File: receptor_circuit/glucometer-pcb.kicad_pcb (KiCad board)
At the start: 2 copper layers, 22 parts, among them IC1 RC4558IP, IC2 LM1458N, IC3 RC4558IP, U1 ESP32_DevKit_V1_DOIT

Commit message: change name
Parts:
- removed BZ1: Buzzer, Buzzer_Beeper:MagneticBuzzer_Kingstate_KCG0601
- removed the D1 at (121.1, 136.9)
- removed D2: LED, LED_THT:LED_D3.0mm_FlatTop
- removed the R3 at (114.7, 115.1)
- removed the R4 at (114.6, 119.1)
- removed U1: ESP32_DevKit_V1_DOIT, esp32_devkit_v1_doit:esp32_devkit_v1_doit_own_ESP
- added REF**: MountingHole_2.2mm_M2_ISO7380, MountingHole:MountingHole_2.2mm_M2_ISO7380, F.Cu at (206.9, 121.8)
- added REF**: MountingHole_2.2mm_M2_ISO7380, MountingHole:MountingHole_2.2mm_M2_ISO7380, F.Cu at (177.1, 175.4)
- added TP3: SIGNAL_OUT, TestPoint:TestPoint_Keystone_5015_Micro-Minature, F.Cu at (198.6, 121.8)
- moved TP2 76.4 mm to (189.8, 121.8), turned to 180 degrees
- moved TP1 65.2 mm to (180.5, 121.8), turned to 180 degrees
- moved D1 56.7 mm to (191.6, 174.8)
- moved C1 53.5 mm to (191.6, 136.5)
- moved R4 52.6 mm to (178.5, 164.2)
- moved C2 52.2 mm to (182.8, 159.8)
- moved C3 52.2 mm to (190.4, 131.4)
- moved R1 52.0 mm to (204.7, 127.1)
- moved R2 52.0 mm to (204.8, 130.9)
- moved R3 52.0 mm to (193.9, 149.0)
- moved R5 52.0 mm to (198.7, 159.9)
- moved R6 52.0 mm to (198.6, 156.7)
- moved R7 52.0 mm to (201.0, 152.4)
- moved IC1 52.0 mm to (201.8, 139.4)
- moved IC2 52.0 mm to (179.2, 154.9)
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- renumbered D3 to D1, R5 to R3, R6 to R4, R7 to R5, R8 to R6, R9 to R7
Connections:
- net SIGNAL_OUT renamed Net-(IC3-Pad6)
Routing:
- net Net-(BZ1-Pad1): track 79.1 -> 0.00 mm
- net Net-(R3-Pad2): track 77.4 -> 0.00 mm
- net VCC: track 176.5 -> 111.8 mm
- net Net-(D2-Pad1): track 54.9 -> 0.00 mm
- net Net-(D2-Pad2): track 37.6 -> 0.00 mm
- net Net-(D1-Pad2): track 19.1 -> 0.00 mm
- net Net-(IC3-Pad6): track 98.8 -> 84.2 mm
- net GND: track 112.7 -> 101.5 mm
- net Net-(BZ1-Pad2): track 9.27 -> 0.00 mm
- net /PWD_1.65: track 102.6 -> 96.3 mm
- net Net-(C2-Pad2): track 50.4 -> 55.9 mm
- net Net-(C1-Pad1): track 23.0 -> 19.4 mm
- net /SIGNAL_1: track 71.2 -> 69.6 mm
- net /SIGNAL_2: track 17.5 -> 16.4 mm
- net Net-(C2-Pad1): track 22.1 -> 23.0 mm
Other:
- board outline added: 36.5 x 59.9 mm

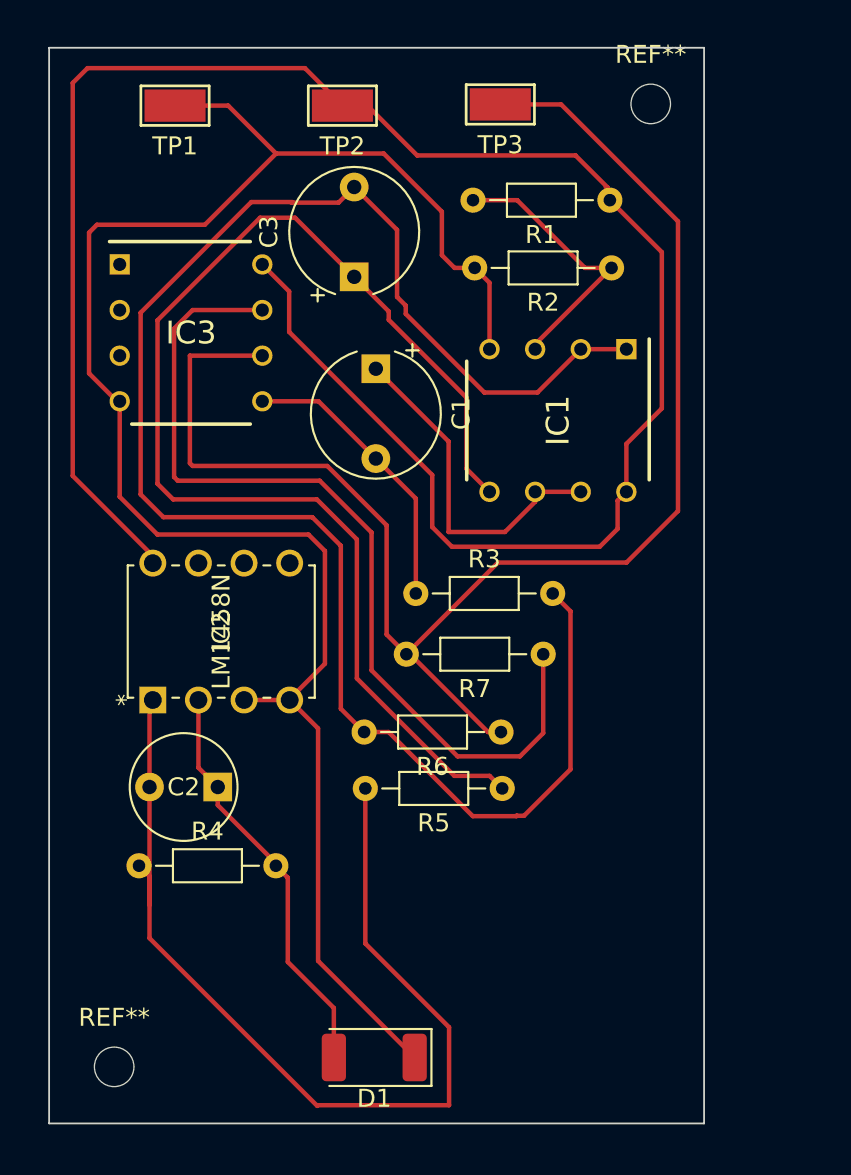
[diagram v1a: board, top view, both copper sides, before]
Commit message: replace top wires with bottom wires
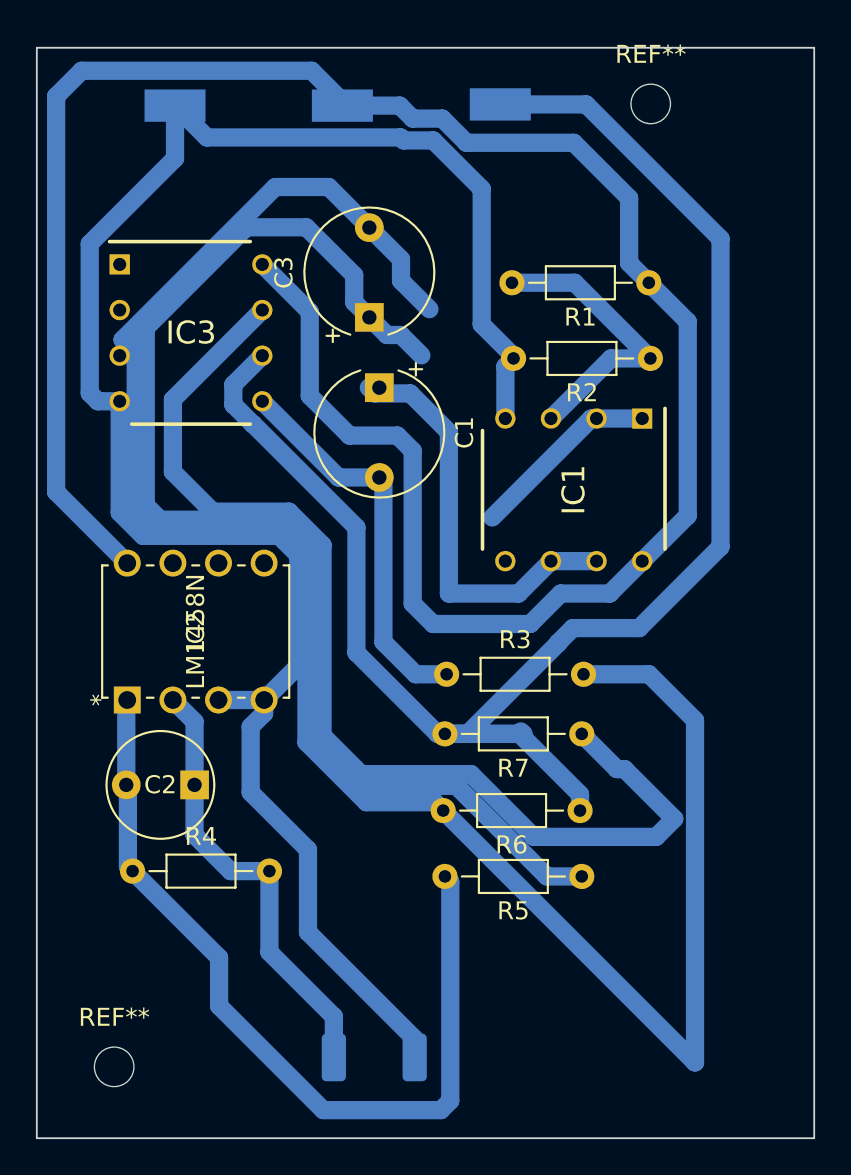
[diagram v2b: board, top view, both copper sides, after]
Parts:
- D1, TP1, TP2, TP3: moved to B.Cu
- moved R5 6.61 mm to (203.1, 164.8)
- moved R6 6.20 mm to (203.0, 161.1)
- moved R2 5.48 mm to (206.9, 135.9)
- moved R1 5.08 mm to (206.8, 131.7)
- moved R7 4.93 mm to (203.1, 156.8)
- moved R3 4.82 mm to (195.6, 153.5)
- moved IC1 3.96 mm to (202.7, 143.2)
- moved C3 2.41 mm to (191.3, 133.6)
- moved IC2 1.42 mm to (177.8, 154.9)
- moved C2 1.30 mm to (181.5, 159.7)
- moved C1 1.07 mm to (191.8, 137.6)
- moved R4 0.47 mm to (178.1, 164.5)
- turned TP1 to 0 degrees
- turned TP2 to 0 degrees
- turned TP3 to 0 degrees
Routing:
- net /PWD_1.65: track 96.3 -> 121.7 mm
- net VCC: track 111.8 -> 124.4 mm
- net Net-(IC3-Pad7): track 50.0 -> 61.2 mm
- net Net-(IC3-Pad6): track 84.2 -> 93.4 mm
- net Net-(C2-Pad2): track 55.9 -> 47.3 mm
- net /SIGNAL_2: track 16.4 -> 21.9 mm
- net Net-(C1-Pad1): track 19.4 -> 23.4 mm
- net GND: track 101.5 -> 105.0 mm
- net Net-(C2-Pad1): track 23.0 -> 24.9 mm
- net Net-(IC1-Pad3): track 15.6 -> 16.4 mm
- net /SIGNAL_1: track 69.6 -> 70.4 mm
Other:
- board size 36.5 x 59.9 mm -> 43.3 x 60.7 mm

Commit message: last update reciver circuit pcb
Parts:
- moved R2 21.0 mm to (205.6, 115.0)
- moved REF** 18.5 mm to (209.9, 103.5)
- moved IC1 16.3 mm to (201.3, 127.0)
- moved R1 15.5 mm to (198.0, 119.0), turned to 0 degrees
- moved TP3 14.1 mm to (205.0, 109.2)
- moved C3 14.1 mm to (184.3, 121.4), turned to 180 degrees
- moved TP2 13.1 mm to (193.3, 109.2)
- moved TP1 12.7 mm to (182.1, 109.2)
- moved R3 5.51 mm to (198.6, 148.9)
- moved C1 4.95 mm to (191.9, 132.6)
- moved R7 4.88 mm to (206.0, 152.9)
- moved R6 3.59 mm to (206.3, 159.7)
- moved R5 3.22 mm to (206.3, 164.7)
- moved REF** 2.48 mm to (174.6, 175.5)
- moved IC3 0.96 mm to (181.3, 133.5)
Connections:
- C1 pad 1: Net-(C1-Pad1) -> /SIGNAL_1
- IC1 pad 6: Net-(C1-Pad1) -> /SIGNAL_1
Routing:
- net Net-(C1-Pad1): track 23.4 -> 0.00 mm
- net /SIGNAL_1: track 70.4 -> 85.2 mm
- net VCC: track 124.4 -> 135.6 mm
- net GND: track 105.0 -> 113.5 mm
- net Net-(IC3-Pad6): track 93.4 -> 86.4 mm
- net Net-(IC1-Pad3): track 16.4 -> 12.2 mm
- net /PWD_1.65: track 121.7 -> 118.1 mm
- net Net-(IC3-Pad7): track 61.2 -> 58.6 mm
- net Net-(C2-Pad2): track 47.3 -> 48.8 mm
- net /SIGNAL_2: track 21.9 -> 21.1 mm
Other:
- board size 43.3 x 60.7 mm -> 43.1 x 79.4 mm

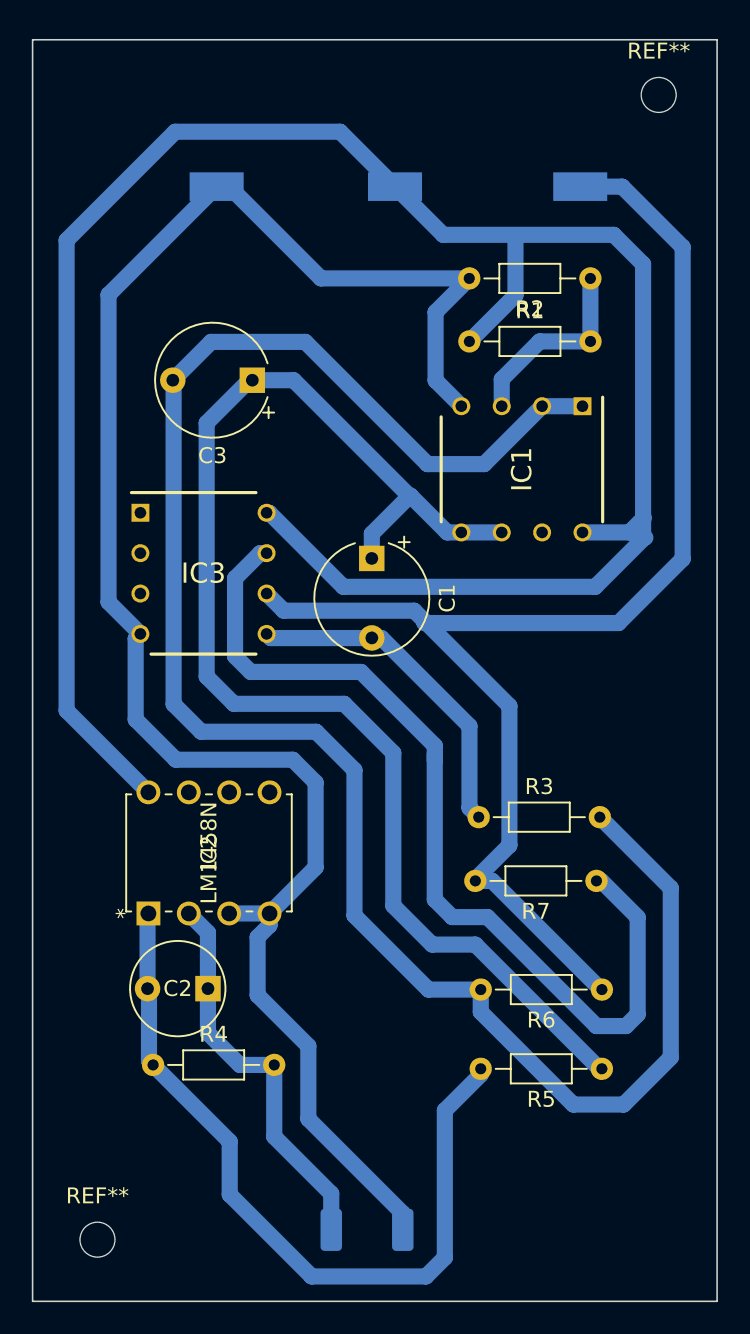
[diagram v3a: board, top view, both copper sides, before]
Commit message: filled pcb
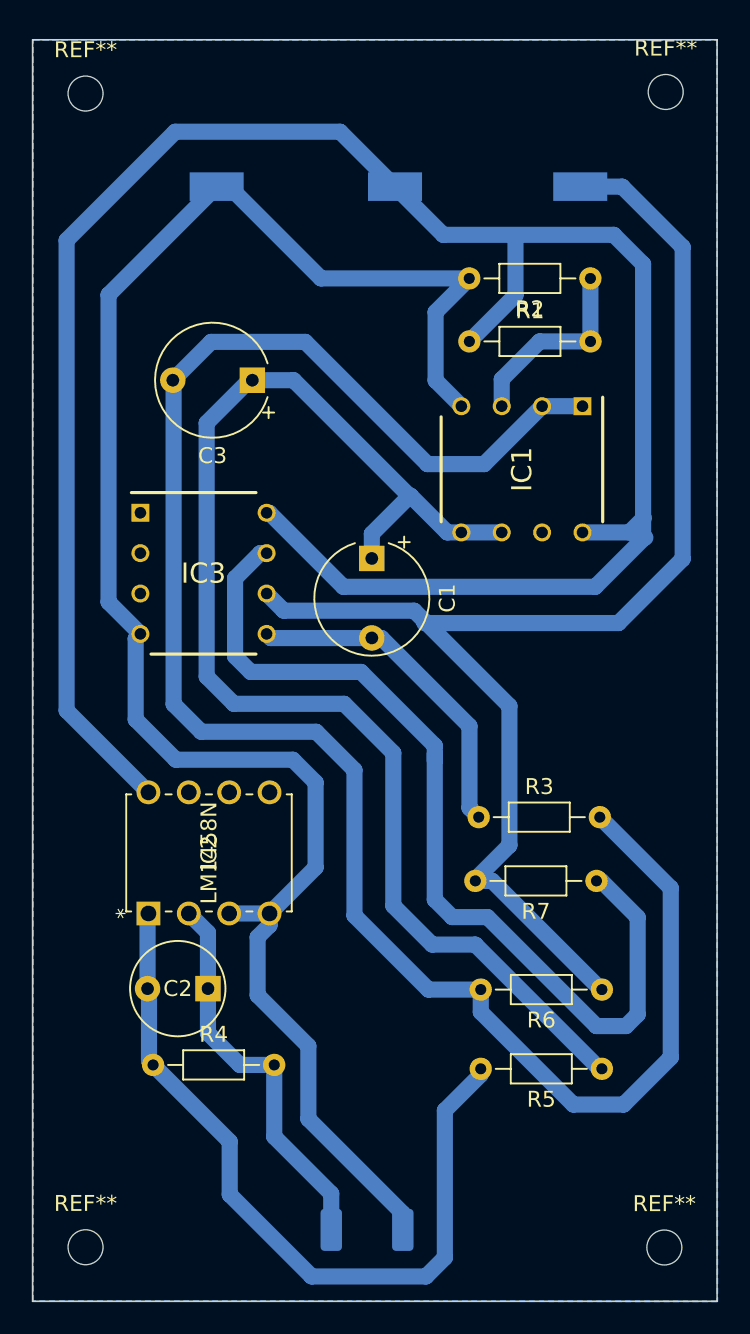
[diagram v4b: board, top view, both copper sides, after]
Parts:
- added REF**: MountingHole_2.2mm_M2_ISO7380, MountingHole:MountingHole_2.2mm_M2_ISO7380, F.Cu at (173.8, 103.4)
- added REF**: MountingHole_2.2mm_M2_ISO7380, MountingHole:MountingHole_2.2mm_M2_ISO7380, F.Cu at (210.3, 176.0)
- moved REF** 0.89 mm to (173.8, 175.9)
- moved REF** 0.48 mm to (210.3, 103.3)
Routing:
- added copper zone on B.Cu, net GND
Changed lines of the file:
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@@
       (net 7 "VCC") (pinfunction "V+") (pintype "passive"))
+  )
+  (footprint "MountingHole:MountingHole_2.2mm_M2_ISO7380" (layer "F.Cu")
+    (at 173.845921 103.364595)
+    (descr "Mounting Hole 2.2mm, no annular, M2, ISO7380")
+    (tags "mounting hole 2.2mm no annular m2 iso7380")
+    (attr exclude_from_pos_files exclude_from_bom)
+    (fp_text reference "REF**" (at 0 -2.75) (layer "F.SilkS")
+      (effects (font (size 1 1) (thickness 0.15)))
+    )
+    (fp_text value "MountingHole_2.2mm_M2_ISO7380" (at 0 2.75) (layer "F.Fab")
+      (effects (font (size 1 1) (thickness 0.15)))
+    )
+    (fp_text user "${REFERENCE}" (at 0 0) (layer "F.Fab")
+      (effects (font (size 1 1) (thickness 0.15)))
+    )
+    (fp_circle (center 0 0) (end 1.75 0) (layer "Cmts.User") (width 0.15) (fill none))
+    (fp_circle (center 0 0) (end 2 0) (layer "F.CrtYd") (width 0.05) (fill none))
+    (pad "" np_thru_hole circle (at 0 0) (size 2.2 2.2) (drill 2.2) (layers *.Cu *.Mask))
+  )
+  (footprint "MountingHole:MountingHole_2.2mm_M2_ISO7380" (layer "F.Cu")
+    (at 210.252776 175.950494)
+    (descr "Mounting Hole 2.2mm, no annular, M2, ISO7380")
+    (tags "mounting hole 2.2mm no annular m2 iso7380")
+    (attr exclude_from_pos_files exclude_from_bom)
+    (fp_text reference "REF**" (at 0 -2.75) (layer "F.SilkS")
+      (effects (font (size 1 1) (thickness 0.15)))
+    )
+    (fp_text value "MountingHole_2.2mm_M2_ISO7380" (at 0 2.75) (layer "F.Fab")
+      (effects (font (size 1 1) (thickness 0.15)))
+    )
+    (fp_text user "${REFERENCE}" (at 0 0) (layer "F.Fab")
+      (effects (font (size 1 1) (thickness 0.15)))
+    )
+    (fp_circle (center 0 0) (end 1.75 0) (layer "Cmts.User") (width 0.15) (fill none))
+    (fp_circle (center 0 0) (end 2 0) (layer "F.CrtYd") (width 0.05) (fill none))
+    (pad "" np_thru_hole circle (at 0 0) (size 2.2 2.2) (drill 2.2) (layers *.Cu *.Mask))
   )
   (footprint "Resistor_THT:R_Axial_DIN0204_L3.6mm_D1.6mm_P7.62mm_Horizontal" (layer "F.Cu")
@@
   )
   (footprint "MountingHole:MountingHole_2.2mm_M2_ISO7380" (layer "F.Cu")
-    (at 209.897992 103.451872)
+    (at 210.33914 103.265307)
     (descr "Mounting Hole 2.2mm, no annular, M2, ISO7380")
     (tags "mounting hole 2.2mm no annular m2 iso7380")
@@
   )
   (footprint "MountingHole:MountingHole_2.2mm_M2_ISO7380" (layer "F.Cu")
-    (at 174.596308 175.458104)
+    (at 173.846036 175.934116)
     (descr "Mounting Hole 2.2mm, no annular, M2, ISO7380")
     (tags "mounting hole 2.2mm no annular m2 iso7380")
@@
   (segment (start 204.961987 109.22) (end 207.602348 109.22) (width 1.016) (layer "B.Cu") (net 17))
   (segment (start 194.516999 135.894274) (end 200.507955 141.88523) (width 1.016) (layer "B.Cu") (net 17))
+  (zone (net 8) (net_name "GND") (layer "B.Cu") (hatch edge 0.508)
+    (connect_pads (clearance 0.508))
+    (min_thickness 0.254) (filled_areas_thickness no)
+    (fill yes (thermal_gap 0.508) (thermal_bridge_width 0.508))
+    (polygon
+      (pts
+        (xy 213.570984 179.31525)
+        (xy 170.534443 179.326242)
+        (xy 170.533435 100.006232)
+        (xy 213.572779 99.993445)
+      )
+    )
+  )
+  (zone (net 8) (net_name "GND") (layer "B.Cu") (hatch edge 0.508)
+    (connect_pads (clearance 1))
+    (min_thickness 0.254) (filled_areas_thickness no)
+    (fill yes (thermal_gap 0.508) (thermal_bridge_width 0.508))
+    (polygon
+      (pts
+        (xy 213.602951 179.355406)
+        (xy 170.538033 179.308857)
+        (xy 170.555419 100.016216)
+        (xy 213.56459 99.97606)
+      )
+    )
+  )
 )

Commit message: fixed PCB
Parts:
- moved REF** 34.6 mm to (175.8, 173.0)
- moved REF** 32.6 mm to (206.3, 172.9)
- moved R4 29.8 mm to (177.3, 124.3), turned to 0 degrees
- moved R3 20.7 mm to (177.3, 120.4)
- moved C2 9.78 mm to (191.4, 128.2), turned to 90 degrees
- moved REF** 8.79 mm to (206.3, 111.1)
- moved REF** 7.94 mm to (175.8, 111.1)
- moved S_OUT1 6.56 mm to (202.5, 115.3)
- moved VCC1 6.12 mm to (192.5, 115.3)
- moved GND1 6.10 mm to (181.4, 115.3)
- moved R2 3.00 mm to (204.3, 162.5)
- moved R5 3.00 mm to (196.6, 146.7)
- moved R6 3.00 mm to (204.3, 157.5)
- moved R7 3.00 mm to (204.0, 150.7)
- moved RECEPTOR_DIODE1 2.55 mm to (191.5, 172.3)
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- renumbered C2 to C1, C3 to C2, C1 to C3, TP1 to GND1, IC2 to LM1458N1, R4 to R1, R5 to R2, R1 to R3, R2 to R4, R3 to R5, IC1 to RC4558IP1, IC3 to RC4558IP2, D1 to RECEPTOR_DIODE1, TP3 to S_OUT1, TP2 to VCC1
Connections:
- C3 pad 1: /SIGNAL_1 -> Net-(C3-Pad1)
- RC4558IP1 pad 6: /SIGNAL_1 -> Net-(C3-Pad1)
- RC4558IP1 pad 7: Net-(C1-Pad1) (its old number) -> Net-(C3-Pad1)
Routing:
- net /SIGNAL_1: track 85.2 -> 66.4 mm
- net /PWD_1.65: track 118.1 -> 102.4 mm
- net VCC: track 135.6 -> 119.9 mm
- net Net-(R3-Pad2): track 12.2 -> 26.1 mm
- net Net-(R6-Pad1): track 86.4 -> 72.7 mm
- net Net-(C3-Pad1): track 0.00 -> 12.3 mm
- net GND: track 113.5 -> 103.5 mm
- net Net-(R7-Pad1): track 58.6 -> 55.5 mm
- net /SIGNAL_2: track 21.1 -> 18.1 mm
- net Net-(C1-Pad2): track 48.8 -> 46.9 mm
- net Net-(C1-Pad1): track 24.9 -> 24.3 mm
- removed copper zone on B.Cu, net GND
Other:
- board size 43.1 x 79.4 mm -> 36.9 x 68.2 mm

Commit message: filled zone
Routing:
- added copper zone on B.Cu, net GND
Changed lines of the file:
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@@
   (segment (start 200.031141 132.634489) (end 198.507094 134.158536) (width 0.25) (layer "B.Cu") (net 4))
   (segment (start 187.93263 140.464412) (end 182.583884 140.464412) (width 0.3) (layer "B.Cu") (net 5))
-  (segment (start 204.297807 162.49408) (end 197.284171 155.480444) (width 0.3) (layer "B.Cu") (net 5))
   (segment (start 204.297807 162.49408) (end 204.153157 162.49408) (width 0.3) (layer "B.Cu") (net 5))
   (segment (start 191.201485 143.733267) (end 187.93263 140.464412) (width 0.3) (layer "B.Cu") (net 5))
@@
   (segment (start 193.882535 155.478452) (end 191.201485 152.797402) (width 0.3) (layer "B.Cu") (net 5))
   (segment (start 197.306235 155.478452) (end 193.882535 155.478452) (width 0.3) (layer "B.Cu") (net 5))
+  (segment (start 204.297807 162.49408) (end 197.284171 155.480444) (width 0.3) (layer "B.Cu") (net 5))
   (segment (start 197.491141 132.634489) (end 193.046426 128.189774) (width 0.25) (layer "B.Cu") (net 5))
   (segment (start 205.187383 164.594522) (end 202.830187 164.594522) (width 0.3) (layer "B.Cu") (net 6))
@@
   (segment (start 205.641516 159.565867) (end 203.944052 159.565867) (width 0.3) (layer "B.Cu") (net 14))
   (segment (start 206.245698 158.961685) (end 205.641516 159.565867) (width 0.3) (layer "B.Cu") (net 14))
+  (zone (net 8) (net_name "GND") (layer "B.Cu") (hatch edge 0.508)
+    (connect_pads (clearance 0.508))
+    (min_thickness 0.254) (filled_areas_thickness no)
+    (fill yes (thermal_gap 0.508) (thermal_bridge_width 0.508))
+    (polygon
+      (pts
+        (xy 209.532853 107.900727)
+        (xy 209.53372 176.101312)
+        (xy 172.642584 176.140236)
+        (xy 172.631586 107.900294)
+      )
+    )
+  )
 )

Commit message: last update
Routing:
- net GND: track 103.5 -> 3.16 mm
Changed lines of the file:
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@@
   (segment (start 206.531781 122.58851) (end 207.250455 123.307184) (width 0.3) (layer "B.Cu") (net 7))
   (segment (start 200.570295 122.58851) (end 206.531781 122.58851) (width 0.3) (layer "B.Cu") (net 7))
-  (segment (start 180.34 127) (end 175.26 127) (width 0.3) (layer "B.Cu") (net 8))
   (segment (start 176.997647 137.651809) (end 177.294626 137.35483) (width 0.3) (layer "B.Cu") (net 8))
-  (segment (start 190.072645 168.581542) (end 193.779544 172.288441) (width 0.3) (layer "B.Cu") (net 8))
-  (segment (start 194.198781 121.402129) (end 197.491141 124.694489) (width 0.3) (layer "B.Cu") (net 8))
-  (segment (start 175.291271 118.226675) (end 178.231558 115.286388) (width 0.3) (layer "B.Cu") (net 8))
-  (segment (start 178.231558 115.286388) (end 181.441249 115.286388) (width 0.3) (layer "B.Cu") (net 8))
-  (segment (start 177.294626 137.35483) (end 175.291271 135.351475) (width 0.3) (layer "B.Cu") (net 8))
-  (segment (start 175.291271 135.351475) (end 175.291271 118.226675) (width 0.3) (layer "B.Cu") (net 8))
-  (segment (start 186.83116 142.988035) (end 180.981141 142.988035) (width 0.3) (layer "B.Cu") (net 8))
-  (segment (start 190.072645 161.220175) (end 190.072645 168.581542) (width 0.3) (layer "B.Cu") (net 8))
-  (segment (start 187.943622 149.956493) (end 187.943622 144.100497) (width 0.3) (layer "B.Cu") (net 8))
-  (segment (start 184.963764 124.342925) (end 182.997075 124.342925) (width 0.3) (layer "B.Cu") (net 8))
   (segment (start 182.849127 152.510988) (end 185.389127 152.510988) (width 0.3) (layer "B.Cu") (net 8))
-  (segment (start 180.981141 142.988035) (end 176.997647 139.004541) (width 0.3) (layer "B.Cu") (net 8))
-  (segment (start 185.389127 152.510988) (end 185.389127 156.536657) (width 0.3) (layer "B.Cu") (net 8))
-  (segment (start 185.389127 156.536657) (end 190.072645 161.220175) (width 0.3) (layer "B.Cu") (net 8))
   (segment (start 184.963764 124.342925) (end 184.825853 124.480836) (width 0.3) (layer "B.Cu") (net 8))
-  (segment (start 185.389127 152.510988) (end 187.943622 149.956493) (width 0.3) (layer "B.Cu") (net 8))
-  (segment (start 187.943622 144.100497) (end 186.83116 142.988035) (width 0.3) (layer "B.Cu") (net 8))
-  (segment (start 182.997075 124.342925) (end 180.34 127) (width 0.3) (layer "B.Cu") (net 8))
-  (segment (start 187.90456 121.402129) (end 194.198781 121.402129) (width 0.3) (layer "B.Cu") (net 8))
-  (segment (start 176.997647 139.004541) (end 176.997647 137.651809) (width 0.3) (layer "B.Cu") (net 8))
-  (segment (start 184.963764 124.342925) (end 187.90456 121.402129) (width 0.3) (layer "B.Cu") (net 8))
   (segment (start 195.731811 120.395159) (end 184.012036 120.395159) (width 0.25) (layer "B.Cu") (net 12))
   (segment (start 180.06427 124.342925) (end 177.343764 124.342925) (width 0.25) (layer "B.Cu") (net 12))
